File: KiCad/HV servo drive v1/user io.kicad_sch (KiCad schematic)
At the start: 14 parts, among them SW1 SW_DIP_x04, U1 TCA9555PWR

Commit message: KiCad 8.0 update
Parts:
- renumbered R87 to R11, R88 to R12, R89 to R13, R11 to R14, R12 to R81, R13 to R82, R14 to R83

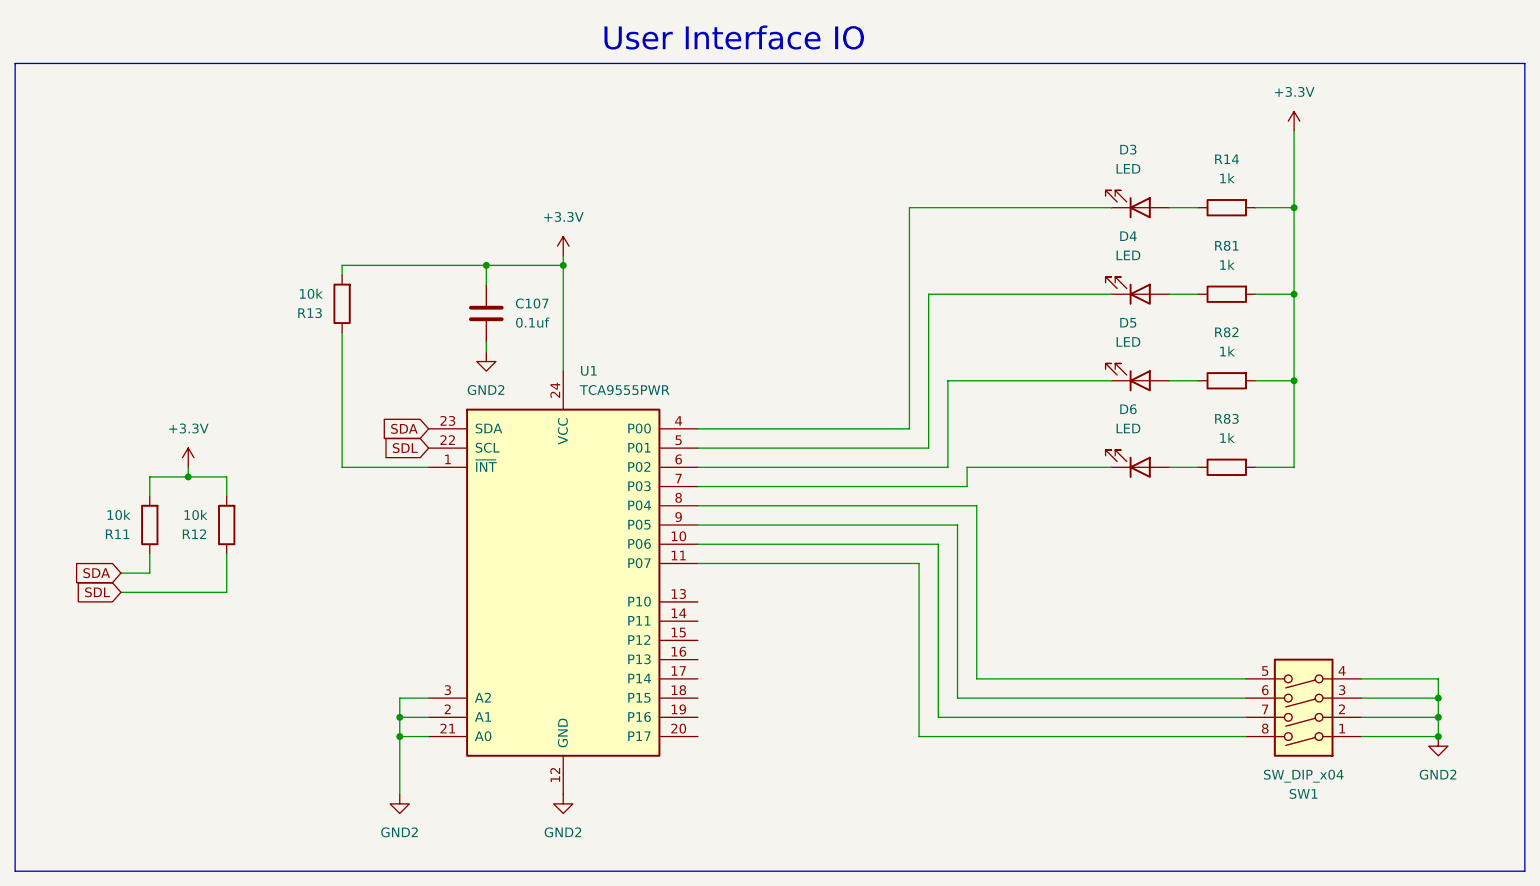
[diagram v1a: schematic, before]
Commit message: start rev 2 changes
fix component references, fix rj45 and dc-dc converter footprints, add RLC filters on all power connectors, add more mounting holes
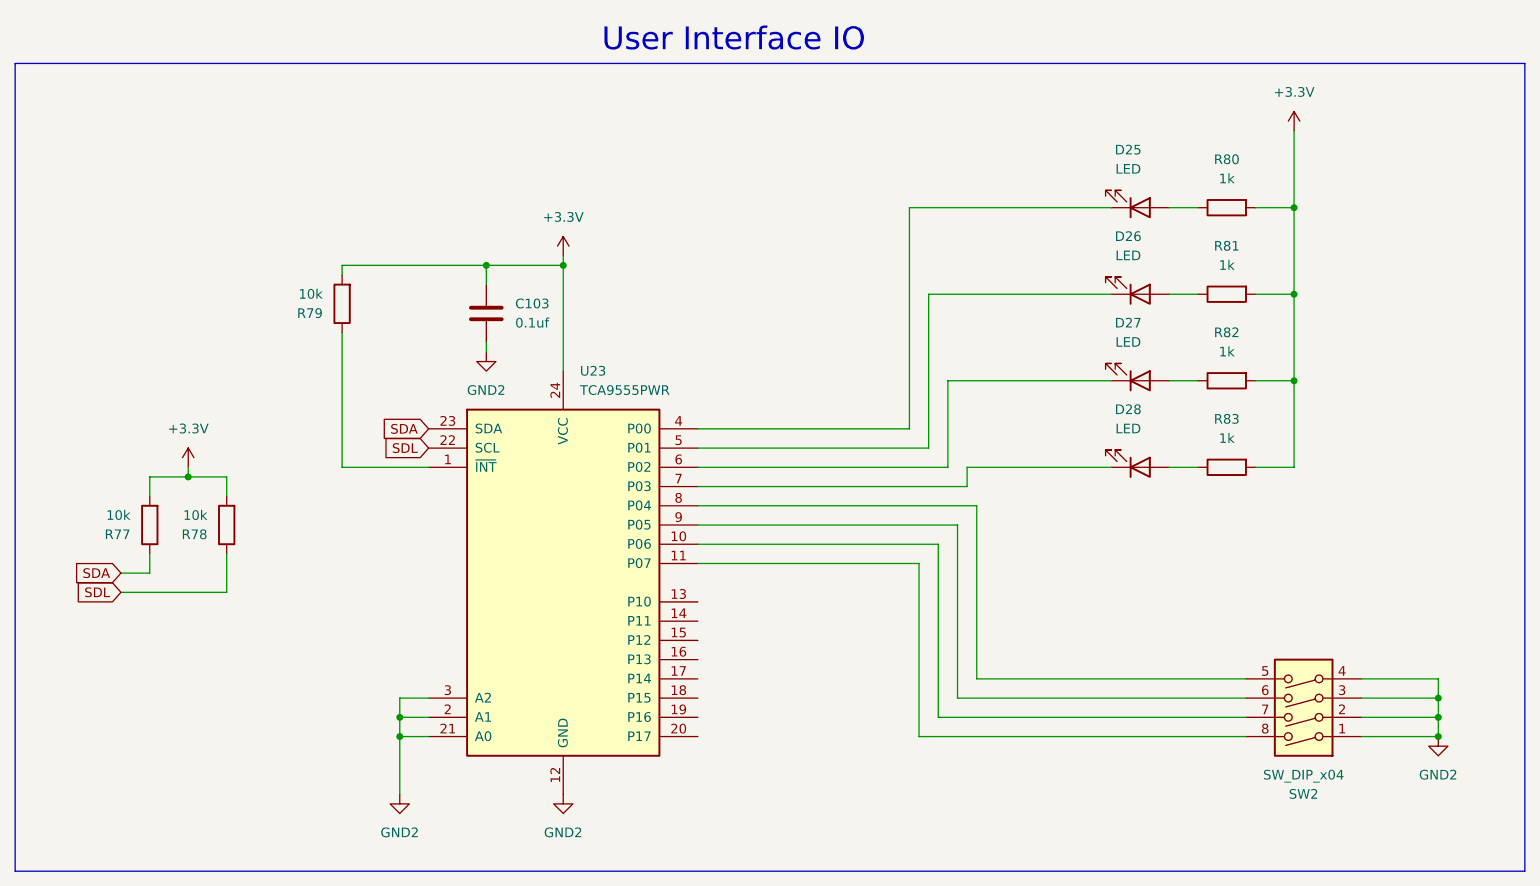
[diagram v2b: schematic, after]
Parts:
- renumbered C107 to C103, D3 to D25, D4 to D26, D5 to D27, D6 to D28, R11 to R77, R12 to R78, R13 to R79, R14 to R80, SW1 to SW2, U1 to U23
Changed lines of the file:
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@@
 		(dnp no)
 		(fields_autoplaced yes)
-		(property "Reference" "C107"
+		(property "Reference" "C103"
 			(at 113.03 71.1199 0)
 			(effects
@@
 			(project "HV servo drive v1"
 				(path "/00e1489f-e855-42b2-9b8a-dcc958a4feb6/350b799a-1897-4e91-b3ab-5fc22b52db7c"
-					(reference "C107")
+					(reference "C103")
 					(unit 1)
 				)
@@
 		(dnp no)
 		(fields_autoplaced yes)
-		(property "Reference" "D3"
+		(property "Reference" "D25"
 			(at 193.9925 50.8 0)
 			(effects
@@
 			(project "HV servo drive v1"
 				(path "/00e1489f-e855-42b2-9b8a-dcc958a4feb6/350b799a-1897-4e91-b3ab-5fc22b52db7c"
-					(reference "D3")
+					(reference "D25")
 					(unit 1)
 				)
@@
 		(dnp no)
 		(fields_autoplaced yes)
-		(property "Reference" "D4"
+		(property "Reference" "D26"
 			(at 193.9925 62.23 0)
 			(effects
@@
 			(project "HV servo drive v1"
 				(path "/00e1489f-e855-42b2-9b8a-dcc958a4feb6/350b799a-1897-4e91-b3ab-5fc22b52db7c"
-					(reference "D4")
+					(reference "D26")
 					(unit 1)
 				)
@@
 		(dnp no)
 		(fields_autoplaced yes)
-		(property "Reference" "U1"
+		(property "Reference" "U23"
 			(at 121.5741 80.01 0)
 			(effects
@@
 			(project "HV servo drive v1"
 				(path "/00e1489f-e855-42b2-9b8a-dcc958a4feb6/350b799a-1897-4e91-b3ab-5fc22b52db7c"
-					(reference "U1")
+					(reference "U23")
 					(unit 1)
 				)
@@
 		(dnp no)
 		(fields_autoplaced yes)
-		(property "Reference" "D5"
+		(property "Reference" "D27"
 			(at 193.9925 73.66 0)
 			(effects
@@
 			(project "HV servo drive v1"
 				(path "/00e1489f-e855-42b2-9b8a-dcc958a4feb6/350b799a-1897-4e91-b3ab-5fc22b52db7c"
-					(reference "D5")
+					(reference "D27")
 					(unit 1)
 				)
@@
 		(dnp no)
 		(fields_autoplaced yes)
-		(property "Reference" "R12"
+		(property "Reference" "R78"
 			(at 72.39 101.6001 0)
 			(effects
@@
 			(project "HV servo drive v1"
 				(path "/00e1489f-e855-42b2-9b8a-dcc958a4feb6/350b799a-1897-4e91-b3ab-5fc22b52db7c"
-					(reference "R12")
+					(reference "R78")
 					(unit 1)
 				)
@@
 		(dnp no)
 		(fields_autoplaced yes)
-		(property "Reference" "#PWR05"
+		(property "Reference" "#PWR0121"
 			(at 97.79 142.24 0)
 			(effects
@@
 			(project "HV servo drive v1"
 				(path "/00e1489f-e855-42b2-9b8a-dcc958a4feb6/350b799a-1897-4e91-b3ab-5fc22b52db7c"
-					(reference "#PWR05")
+					(reference "#PWR0121")
 					(unit 1)
 				)
@@
 		(dnp no)
 		(fields_autoplaced yes)
-		(property "Reference" "R11"
+		(property "Reference" "R77"
 			(at 62.23 101.6001 0)
 			(effects
@@
 			(project "HV servo drive v1"
 				(path "/00e1489f-e855-42b2-9b8a-dcc958a4feb6/350b799a-1897-4e91-b3ab-5fc22b52db7c"
-					(reference "R11")
+					(reference "R77")
 					(unit 1)
 				)
@@
 		(dnp no)
 		(fields_autoplaced yes)
-		(property "Reference" "R13"
+		(property "Reference" "R79"
 			(at 87.63 72.3901 0)
 			(effects
@@
 			(project "HV servo drive v1"
 				(path "/00e1489f-e855-42b2-9b8a-dcc958a4feb6/350b799a-1897-4e91-b3ab-5fc22b52db7c"
-					(reference "R13")
+					(reference "R79")
 					(unit 1)
 				)
@@
 		(dnp no)
 		(fields_autoplaced yes)
-		(property "Reference" "#PWR012"
+		(property "Reference" "#PWR0123"
 			(at 119.38 68.58 0)
 			(effects
@@
 			(project "HV servo drive v1"
 				(path "/00e1489f-e855-42b2-9b8a-dcc958a4feb6/350b799a-1897-4e91-b3ab-5fc22b52db7c"
-					(reference "#PWR012")
+					(reference "#PWR0123")
 					(unit 1)
 				)
@@
 		(dnp no)
 		(fields_autoplaced yes)
-		(property "Reference" "#PWR04"
+		(property "Reference" "#PWR0120"
 			(at 69.85 96.52 0)
 			(effects
@@
 			(project "HV servo drive v1"
 				(path "/00e1489f-e855-42b2-9b8a-dcc958a4feb6/350b799a-1897-4e91-b3ab-5fc22b52db7c"
-					(reference "#PWR04")
+					(reference "#PWR0120")
 					(unit 1)
 				)
@@
 		(dnp no)
 		(fields_autoplaced yes)
-		(property "Reference" "D6"
+		(property "Reference" "D28"
 			(at 193.9925 85.09 0)
 			(effects
@@
 			(project "HV servo drive v1"
 				(path "/00e1489f-e855-42b2-9b8a-dcc958a4feb6/350b799a-1897-4e91-b3ab-5fc22b52db7c"
-					(reference "D6")
+					(reference "D28")
 					(unit 1)
 				)
@@
 		(dnp no)
 		(fields_autoplaced yes)
-		(property "Reference" "#PWR044"
+		(property "Reference" "#PWR0125"
 			(at 215.9 52.07 0)
 			(effects
@@
 			(project "HV servo drive v1"
 				(path "/00e1489f-e855-42b2-9b8a-dcc958a4feb6/350b799a-1897-4e91-b3ab-5fc22b52db7c"
-					(reference "#PWR044")
+					(reference "#PWR0125")
 					(unit 1)
 				)
@@
 		(dnp no)
 		(fields_autoplaced yes)
-		(property "Reference" "SW1"
+		(property "Reference" "SW2"
 			(at 217.17 135.89 0)
 			(effects
@@
 			(project "HV servo drive v1"
 				(path "/00e1489f-e855-42b2-9b8a-dcc958a4feb6/350b799a-1897-4e91-b3ab-5fc22b52db7c"
-					(reference "SW1")
+					(reference "SW2")
 					(unit 1)
 				)
@@
 		(dnp no)
 		(fields_autoplaced yes)
-		(property "Reference" "#PWR042"
+		(property "Reference" "#PWR0124"
 			(at 119.38 142.24 0)
 			(effects
@@
 			(project "HV servo drive v1"
 				(path "/00e1489f-e855-42b2-9b8a-dcc958a4feb6/350b799a-1897-4e91-b3ab-5fc22b52db7c"
-					(reference "#PWR042")
+					(reference "#PWR0124")
 					(unit 1)
 				)
@@
 		(dnp no)
 		(fields_autoplaced yes)
-		(property "Reference" "#PWR07"
+		(property "Reference" "#PWR0122"
 			(at 109.22 83.82 0)
 			(effects
@@
 			(project "HV servo drive v1"
 				(path "/00e1489f-e855-42b2-9b8a-dcc958a4feb6/350b799a-1897-4e91-b3ab-5fc22b52db7c"
-					(reference "#PWR07")
+					(reference "#PWR0122")
 					(unit 1)
 				)
@@
 		(dnp no)
 		(fields_autoplaced yes)
-		(property "Reference" "R14"
+		(property "Reference" "R80"
 			(at 207.01 52.07 90)
 			(effects
@@
 			(project "HV servo drive v1"
 				(path "/00e1489f-e855-42b2-9b8a-dcc958a4feb6/350b799a-1897-4e91-b3ab-5fc22b52db7c"
-					(reference "R14")
+					(reference "R80")
 					(unit 1)
 				)
@@
 		(dnp no)
 		(fields_autoplaced yes)
-		(property "Reference" "#PWR0129"
+		(property "Reference" "#PWR0126"
 			(at 234.95 134.62 0)
 			(effects
@@
 			(project "HV servo drive v1"
 				(path "/00e1489f-e855-42b2-9b8a-dcc958a4feb6/350b799a-1897-4e91-b3ab-5fc22b52db7c"
-					(reference "#PWR0129")
-					(unit 1)
-				)
+					(reference "#PWR0126")
+					(unit 1)
+				)

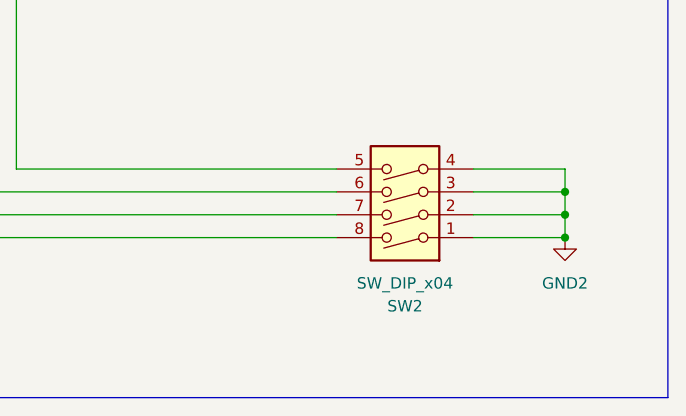
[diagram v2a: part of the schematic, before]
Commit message: update to rev 2.1
basically the same version as in the FOC youtube video, with some minor issues fixed
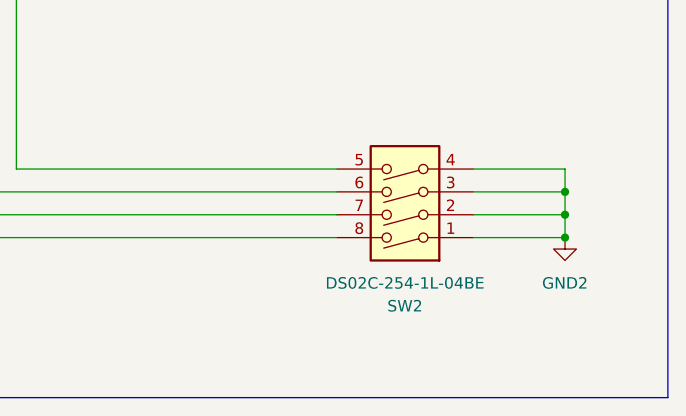
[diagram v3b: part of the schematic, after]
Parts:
- C103: Generic Allowed? (none) -> yes; Manufacturer (none) -> YAGEO; Part number (none) -> CC0603ZRY5V9BB104
- D25, D26, D27, D28: Generic Allowed? (none) -> yes; Manufacturer (none) -> Harvatek Corporation; Part number (none) -> B1931NG--20D001114U1930
- R77, R78, R79: Generic Allowed? (none) -> yes; Manufacturer (none) -> YAGEO; Part number (none) -> RC0603FR-0710KL
- R80, R81, R82, R83: Generic Allowed? (none) -> yes; Manufacturer (none) -> YAGEO; Part number (none) -> RC0603FR-071KL
- SW2: value SW_DIP_x04 -> DS02C-254-1L-04BE; Generic Allowed? (none) -> yes; Manufacturer (none) -> Same Sky (Formerly CUI Devices); Part number (none) -> DS02C-254-1L-04BE
- U23: Generic Allowed? (none) -> no; Manufacturer (none) -> Texas Instruments; Part number (none) -> TCA9555PWR
